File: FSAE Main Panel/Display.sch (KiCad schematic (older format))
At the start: 82 parts, among them Q501 SI2308CDS-T1-GE3, Q502 SI2308CDS-T1-GE3, U501 TLC6C598, U502 TLC6C5816, U503 TLC6C5816, U504 TLC6C5816

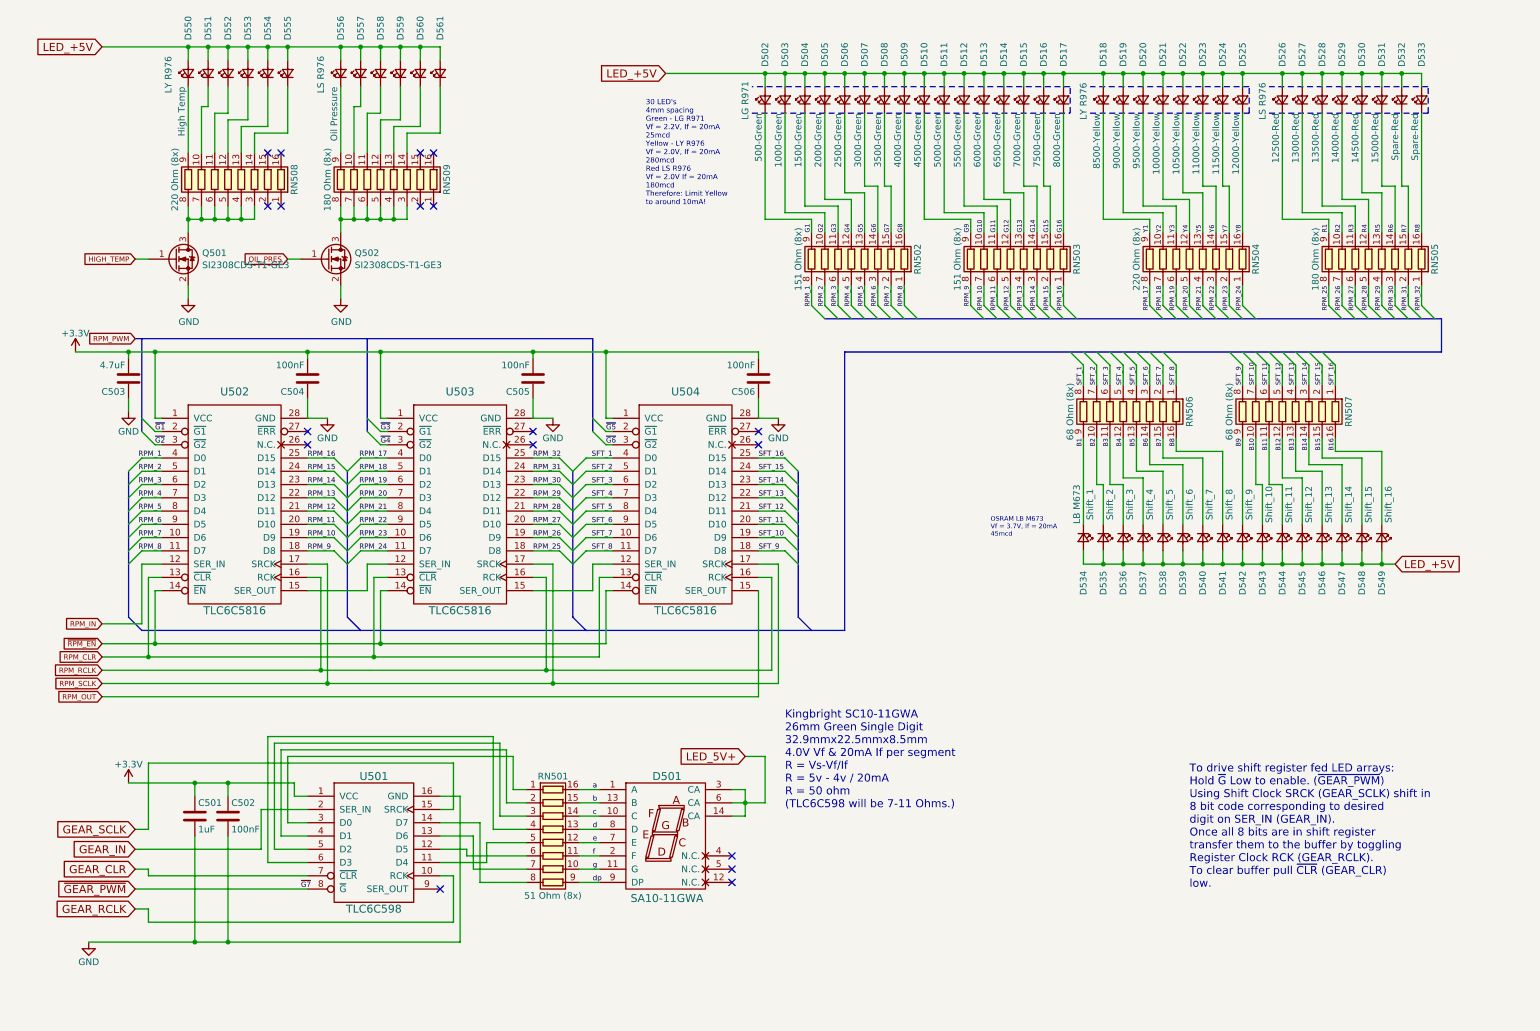
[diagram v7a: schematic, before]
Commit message: Major Revision
Deleted a ton of routes, Sorry Gary.
Changed all LEDs to 1206s for better brightness
Added a lot of local net names for easier routing
Flipped J203 for better routing
Expanded board outline to fit final dashboard cutout
Added half of the Mounting Holes
Realigned RPM strip
Added Linear Reg Load Resistors to meet minimum current specs
Changed Aux load Linear Regulators to a better one
Added Separate Linear Reg for the DWC
Tuned the CAN Bus differential Pair Lines for equal length
Added decoupling capacitors at a few locations
Rerouted Power traces to be shorter and cleaner
Set up keep out zones for CAN bus interference shielding.
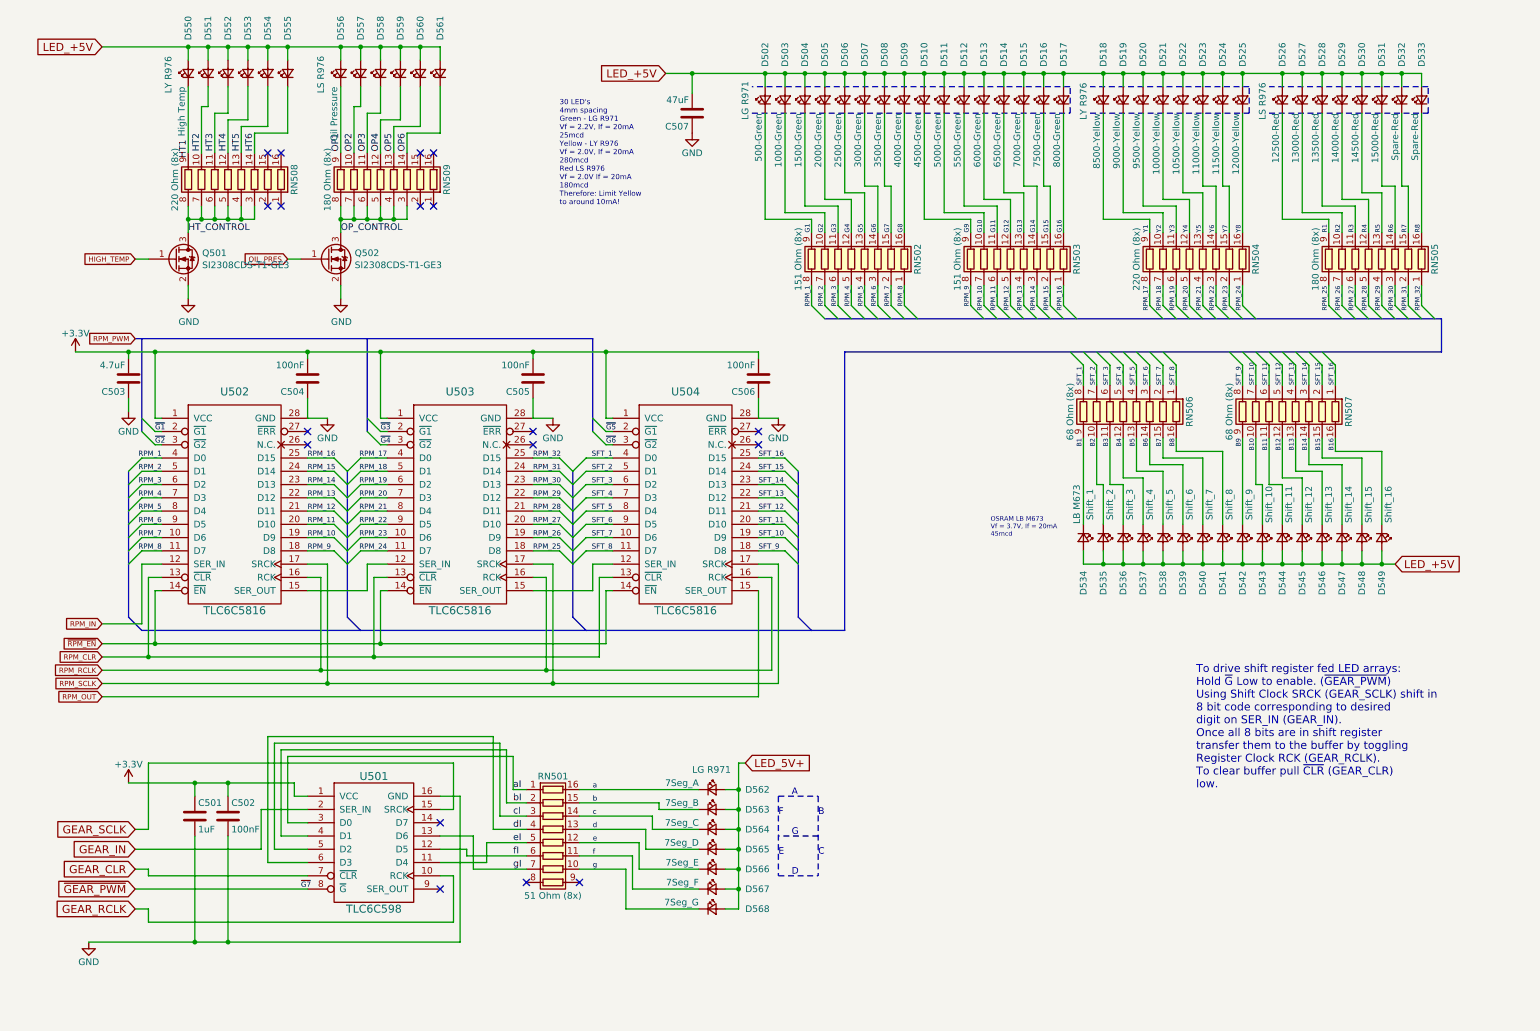
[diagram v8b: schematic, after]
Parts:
- removed D501: SA10-11GWA, Kingbright:SC10-11EWA, symbol KingBright_Addition:SA10-11GWA
- added C507: 47uF, Capacitors_SMD:C_1206, symbol Device:C
- added D562, D563, D564, D565, D566, D567, D568: LG R971, LEDs:LED_1206, symbol Device:LED_Small
- D502, D503, D504, D505, D506, D507, D508, D509, D510, D511, D512, D513, D514, D515, D516, D517, D518, D519, D520, D521, D522, D523, D524, D525, D526, D527, D528, D529, D530, D531, D532, D533, D534, D535, D536, D537, D538, D539, D540, D541, D542, D543, D544, D545, D546, D547, D548, D549, D550, D551, D552, D553, D554, D555, D556, D557, D558, D559, D560, D561: footprint LEDs:LED_0805 -> LEDs:LED_1206
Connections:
- net GND: now also C507.1
- net LED_+5V: now also C507.2
- net LED_5V+: now also D562.2 (A), D563.2 (A), D564.2 (A), D565.2 (A), D566.2 (A), D567.2 (A), D568.2 (A)
- net a: now also D562.1 (K)
- net b: now also D563.1 (K)
- net c: now also D564.1 (K)
- net d: now also D565.1 (K)
- net e: now also D566.1 (K)
- net f: now also D567.1 (K)
- net g: now also D568.1 (K)
- net aI: now reaches RN501.1 (R1.1), U501.3 (D0)
- net bI: now reaches RN501.2 (R2.1), U501.4 (D1)
- net cI: now reaches RN501.3 (R3.1), U501.5 (D2)
- net dI: now reaches RN501.4 (R4.1), U501.6 (D3)
- net eI: now reaches RN501.5 (R5.1), U501.11 (D4)
- net fI: now reaches RN501.6 (R6.1), U501.12 (D5)
- net gI: now reaches RN501.7 (R7.1), U501.13 (D6)
- net at RN501.8 (R8.1): no longer U501.14 (D7)
- net HT1: now reaches D550.1 (K), RN508.9 (R8.2)
- net HT2: now reaches D551.1 (K), RN508.10 (R7.2)
- net HT3: now reaches D552.1 (K), RN508.11 (R6.2)
- net HT4: now reaches D553.1 (K), RN508.12 (R5.2)
- net HT5: now reaches D554.1 (K), RN508.13 (R4.2)
- net HT6: now reaches D555.1 (K), RN508.14 (R3.2)
- net HT_CONTROL: now reaches Q501.3 (D), RN508.3 (R3.1), RN508.4 (R4.1), RN508.5 (R5.1), RN508.6 (R6.1), RN508.7 (R7.1), RN508.8 (R8.1)
- net OP2: now reaches D557.1 (K), RN509.10 (R7.2)
- net OP3: now reaches D558.1 (K), RN509.11 (R6.2)
- net OP4: now reaches D559.1 (K), RN509.12 (R5.2)
- net OP5: now reaches D560.1 (K), RN509.13 (R4.2)
- net OP6: now reaches D561.1 (K), RN509.14 (R3.2)
- net OP_CONTROL: now reaches Q502.3 (D), RN509.3 (R3.1), RN509.4 (R4.1), RN509.5 (R5.1), RN509.6 (R6.1), RN509.7 (R7.1), RN509.8 (R8.1)
- net OP1: now reaches D556.1 (K), RN509.9 (R8.2)
- net dp: no longer names the net of RN501.9 (R8.2)
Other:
- note added: "A"
- note added: "B"
- note added: "C"
- note added: "D"
- note added: "E"
- note added: "F"
- note added: "G"
- note removed: "Kingbright SC10-11GWA\n26mm Green Single Digit\n32.9mmx22.5mmx8.5mm\n4.0V Vf & 20mA If per segment\nR = Vs-Vf/If\nR = 5v - 4v / 20mA\nR = 50 ohm\n(TLC6C598 will be 7-11 Ohms.)"
